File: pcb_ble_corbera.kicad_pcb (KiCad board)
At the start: 2 copper layers, 48 x 25 mm, 15 parts, among them J1 Conn_01x02, J2 Conn_02x04_Odd_Even, J4 Conn_ARM_JTAG_SWD_10, SW1 SW_Push, U1 BL652, U2 HDC1080

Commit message: added battery holder 3d model
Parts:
- added REF**: OSHW-Logo2_7.3x6mm_SilkScreen, Symbol:OSHW-Logo2_7.3x6mm_SilkScreen, F.Cu at (137.9, 104.7)
- moved REF** 0.46 mm to (132.2, 95.6)

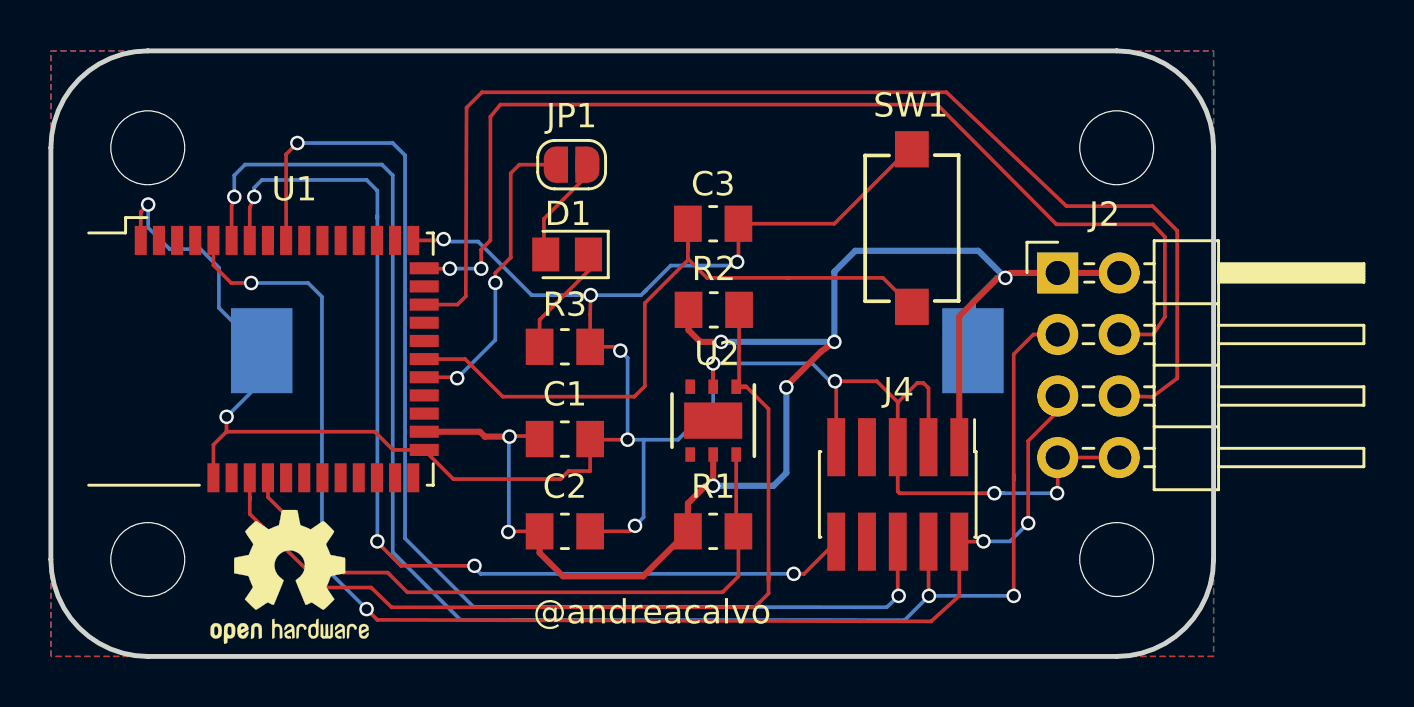
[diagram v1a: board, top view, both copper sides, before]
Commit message: changed hdc1080 with sht20
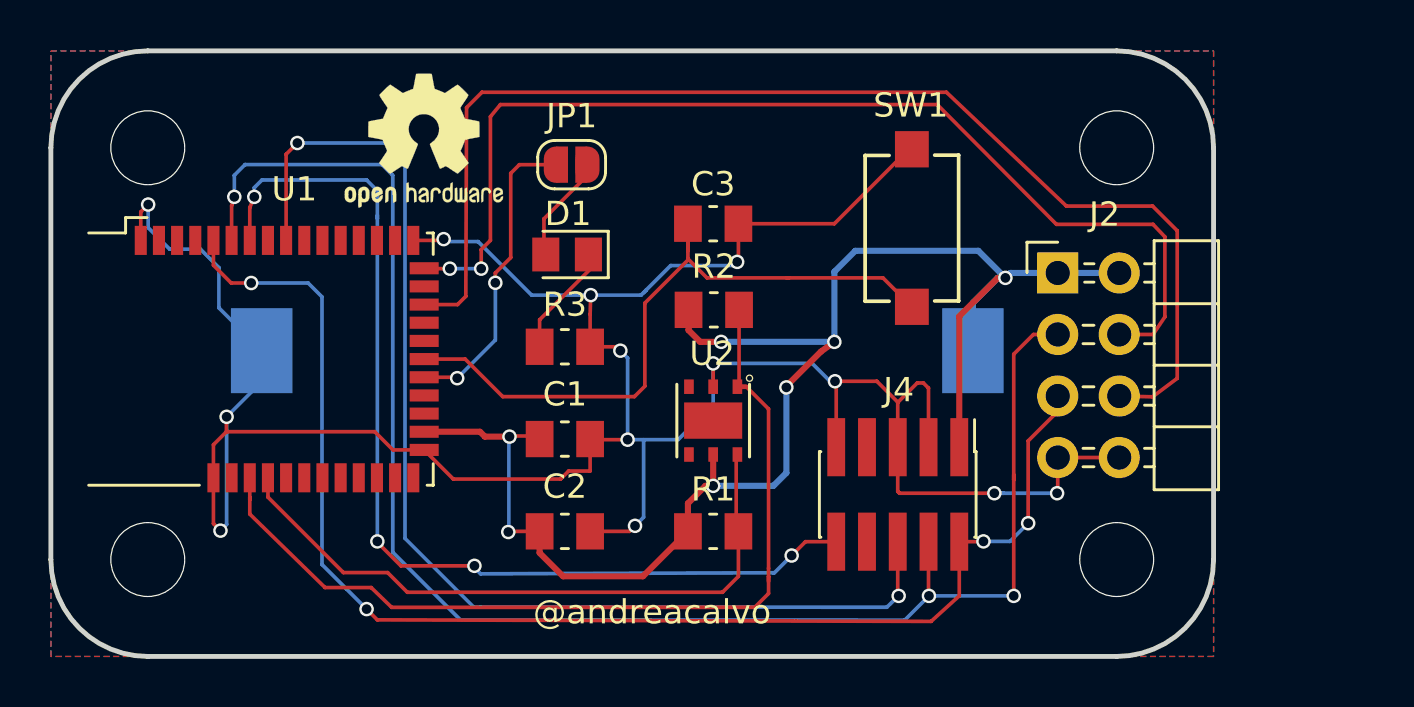
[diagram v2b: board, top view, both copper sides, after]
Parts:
- removed the REF** at (132.2, 95.6)
- J1: value Conn_01x02 -> Battery_Cell
- J2: footprint Connector_PinHeader_2.54mm:PinHeader_2x04_P2.54mm_Horizontal -> _Project:PinHeader_2x04_P2.54mm_Horizontal_No_Pins
- U2: value HDC1080 -> SHT20; footprint Package_SON:Texas_PWSON-N6 -> _Project:SHT20
- moved REF** 18.8 mm to (143.4, 86.7)
- turned J1 to 180 degrees
- turned R1 to 180 degrees
- turned R2 to 180 degrees
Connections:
- J1 pad 1: GND -> VCC
- J1 pad 2: VCC -> GND
- R1 pad 1: VCC -> SCL
- R1 pad 2: SCL -> VCC
- R2 pad 1: VCC -> SDA
- R2 pad 2: SDA -> VCC
- U2 pad 3: Net-(U2-Pad3) -> (no net)
- U2 pad 4: Net-(U2-Pad4) -> (no net)
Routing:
- net GND: track 110.0 -> 117.1 mm, vias 12 -> 13

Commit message: added kicad logo
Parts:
- added REF**: KiCad-Logo2_6mm_SilkScreen, Symbol:KiCad-Logo2_6mm_SilkScreen, B.Cu at (132.0, 95.5)
- moved REF** 18.7 mm to (138.6, 104.8)
